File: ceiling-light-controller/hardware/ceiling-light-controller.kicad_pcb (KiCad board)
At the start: 2 copper layers, 15 parts, among them J1 Screw_Terminal_01x03, J2 Screw_Terminal_01x02, Q1 BT136-500, U1 LTV-817, U2 HLK-PM03, U3 MOC3021M, U4 WeMos_mini

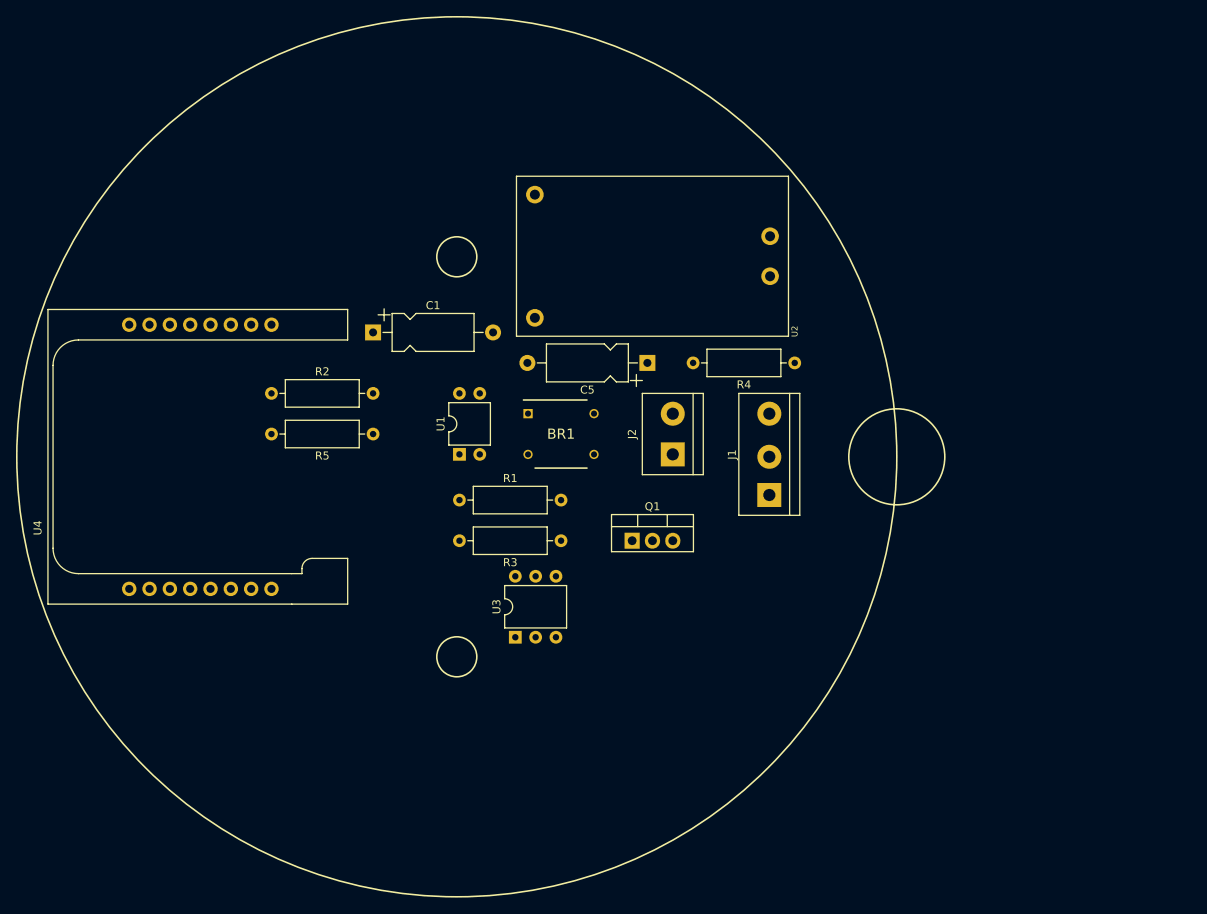
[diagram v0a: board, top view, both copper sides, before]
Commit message: LED, LDR; PCB layout; copper traces
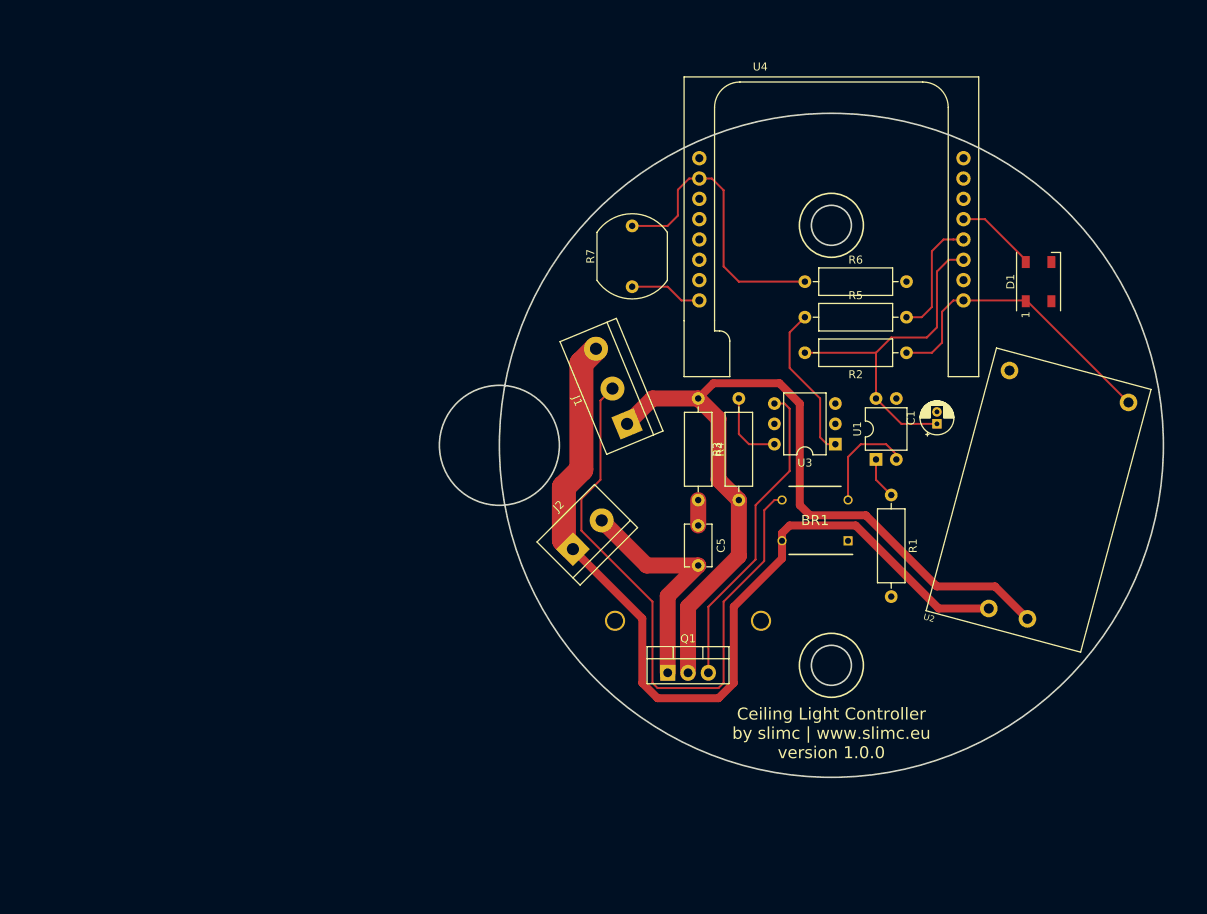
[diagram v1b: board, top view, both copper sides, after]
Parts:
- added D1: WS2812B, LED_SMD:LED_WS2812B_PLCC4_5.0x5.0mm_P3.2mm, F.Cu at (172.7, 78.1)
- added R6: 10000, Resistor_THT:R_Axial_DIN0309_L9.0mm_D3.2mm_P12.70mm_Horizontal, F.Cu at (143.5, 78.1)
- added R7: LDR03, OptoDevice:R_LDR_10x8.5mm_P7.6mm_Vertical, F.Cu at (121.9, 78.7)
- C1: footprint Capacitor_THT:CP_Axial_L10.0mm_D4.5mm_P15.00mm_Horizontal -> Capacitor_THT:CP_Radial_D4.0mm_P1.50mm
- C5: footprint Capacitor_THT:CP_Axial_L10.0mm_D4.5mm_P15.00mm_Horizontal -> Capacitor_THT:C_Disc_D5.1mm_W3.2mm_P5.00mm
- Q1: footprint Package_TO_SOT_THT:TO-220-3_Vertical -> slimc:TO-220-3_Vertical_Triode_Heatsink
- moved U4 83.8 mm to (146.8, 71.6), turned to 90 degrees
- moved R2 79.5 mm to (156.2, 87.0), turned to 180 degrees
- moved C1 71.4 mm to (160.0, 95.9), turned to 90 degrees
- moved U2 57.1 mm to (172.7, 105.4), turned to 75 degrees
- moved R5 55.9 mm to (143.5, 82.5), turned to 0 degrees
- moved R1 54.0 mm to (154.3, 104.8), turned to 270 degrees
- moved U1 52.1 mm to (152.4, 100.3)
- moved U3 46.7 mm to (147.3, 98.4), turned to 180 degrees
- moved BR1 33.5 mm to (144.8, 108.0), turned to 180 degrees
- moved R3 22.8 mm to (135.3, 105.4), turned to 90 degrees
- moved C5 21.3 mm to (130.2, 108.6), turned to 270 degrees
- moved J1 19.9 mm to (121.3, 95.9), turned to 112.5 degrees
- moved J2 17.2 mm to (114.5, 111.5), turned to 45 degrees
- moved Q1 17.1 mm to (126.4, 127.0)
- moved R4 12.9 mm to (130.2, 92.7), turned to 270 degrees
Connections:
- BR1 pad 3: NEUT -> Net-(BR1-Pad3)
- BR1 pad 4: VAC -> Net-(BR1-Pad4)
- C5 pad 2: VAC -> Net-(C5-Pad2)
- J1 pad 1: VAC -> Net-(J1-Pad1)
- J1 pad 2: NEUT -> Net-(BR1-Pad3)
- J1 pad 3: VAC -> Net-(BR1-Pad4)
- J2 pad 1: NEUT -> Net-(BR1-Pad4)
- J2 pad 2: VAC -> Net-(C5-Pad2)
- Q1 pad 1: VAC -> Net-(C5-Pad2)
- Q1 pad 2: VAC -> Net-(J1-Pad1)
- R3 pad 1: VAC -> Net-(J1-Pad1)
- R4 pad 1: VAC -> Net-(J1-Pad1)
- U2 pad 1: NEUT -> Net-(BR1-Pad4)
- U2 pad 2: VAC -> Net-(J1-Pad1)
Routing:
- net Net-(BR1-Pad4): track 0.00 -> 114.8 mm
- net Net-(J1-Pad1): track 0.00 -> 110.8 mm
- net Net-(BR1-Pad3): track 0.00 -> 78.0 mm
- net Net-(C1-Pad1): track 0.00 -> 43.4 mm
- net Net-(Q1-Pad3): track 0.00 -> 39.4 mm
- net Net-(D1-Pad1): track 0.00 -> 38.0 mm
- net Net-(R6-Pad1): track 0.00 -> 36.9 mm
- net Net-(C5-Pad2): track 0.00 -> 29.4 mm
- net Net-(R5-Pad1): track 0.00 -> 19.6 mm
- net Net-(R5-Pad2): track 0.00 -> 15.2 mm
- net Net-(BR1-Pad2): track 0.00 -> 13.2 mm
- net Net-(D1-Pad4): track 0.00 -> 10.2 mm
- net Net-(R3-Pad2): track 0.00 -> 9.42 mm
- net Net-(R7-Pad1): track 0.00 -> 9.11 mm
- net Net-(R1-Pad1): track 0.00 -> 5.23 mm
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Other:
- board outline added: 90.5 x 83 mm
- board text added: "Ceiling Light Controller by slimc | www.slimc.eu version 1.0.0"

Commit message: gerber files and order sample
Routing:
- net Net-(BR1-Pad1): track 0.00 -> 9.70 mm
- added copper zone on B.Cu, net GND
- added copper zone on F.Cu, net GND
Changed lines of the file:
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@@
     (thickness 1.6)
     (drawings 7)
-    (tracks 121)
+    (tracks 125)
     (zones 0)
     (modules 18)
@@
     (visible_elements FFFFFF7F)
     (pcbplotparams
-      (layerselection 0x010fc_ffffffff)
+      (layerselection 0x010a0_ffffffff)
       (usegerberextensions false)
       (usegerberattributes false)
@@
       (outputformat 1)
       (mirror false)
-      (drillshape 1)
+      (drillshape 0)
       (scaleselection 1)
-      (outputdirectory ""))
+      (outputdirectory "gerbers/"))
   )
   (net 0 "")
@@
     )
   )
+  (gr_circle (center 146.825 98.565) (end 188.325 98.565) (layer Edge.Cuts) (width 0.2))
+  (gr_circle (center 105.325 98.565) (end 112.825 98.565) (layer Edge.Cuts) (width 0.2))
   (gr_circle (center 146.825 126.065) (end 150.825 126.065) (layer F.SilkS) (width 0.2))
   (gr_circle (center 146.825 71.065) (end 150.825 71.065) (layer F.SilkS) (width 0.2))
-  (gr_circle (center 105.325 98.565) (end 112.825 98.565) (layer Edge.Cuts) (width 0.2))
   (gr_circle (center 146.825 126.065) (end 149.325 126.065) (layer Edge.Cuts) (width 0.2))
   (gr_circle (center 146.825 71.065) (end 149.325 71.065) (layer Edge.Cuts) (width 0.2))
-  (gr_circle (center 146.825 98.565) (end 188.325 98.565) (layer Edge.Cuts) (width 0.2))
   (gr_text "Ceiling Light Controller\nby slimc | www.slimc.eu\nversion 1.0.0" (at 146.825 134.565) (layer F.SilkS)
     (effects (font (size 1.5 1.5) (thickness 0.3)))
@@
   (segment (start 162.062208 72.835) (end 163.335 72.835) (width 0.25) (layer F.Cu) (net 8))
   (segment (start 158.115 82.55) (end 159.385 81.28) (width 0.25) (layer F.Cu) (net 8))
+  (segment (start 154.305 115.07) (end 154.305 116.34363) (width 0.25) (layer F.Cu) (net 20))
+  (segment (start 154.305 116.34363) (end 154.305 117.475) (width 0.25) (layer F.Cu) (net 20))
+  (segment (start 149.735 110.5) (end 154.305 115.07) (width 0.25) (layer F.Cu) (net 20))
+  (segment (start 148.905 110.5) (end 149.735 110.5) (width 0.25) (layer F.Cu) (net 20))
   (segment (start 154.94 99.695) (end 154.94 100.33) (width 0.25) (layer F.Cu) (net 21))
   (segment (start 153.67 98.425) (end 154.94 99.695) (width 0.25) (layer F.Cu) (net 21))
@@
   (segment (start 139.71 105.4) (end 138.43 106.68) (width 0.25) (layer F.Cu) (net 24))
   (segment (start 138.43 106.68) (end 138.43 113.03) (width 0.25) (layer F.Cu) (net 24))
-  (segment (start 115.57 88.32532) (end 117.396936 86.498384) (width 3) (layer F.Cu) (net 25))
-  (segment (start 113.386528 110.410732) (end 113.386528 103.783472) (width 3) (layer F.Cu) (net 25))
-  (segment (start 114.517898 111.542102) (end 113.386528 110.410732) (width 3) (layer F.Cu) (net 25))
-  (segment (start 115.57 101.6) (end 115.57 88.32532) (width 3) (layer F.Cu) (net 25))
-  (segment (start 113.386528 103.783472) (end 115.57 101.6) (width 3) (layer F.Cu) (net 25))
   (segment (start 114.517898 111.542102) (end 115.649268 112.673472) (width 0.25) (layer F.Cu) (net 25))
   (segment (start 125.09359 130.175) (end 132.71641 130.175) (width 1) (layer F.Cu) (net 25))
@@
   (segment (start 123.19 120.214204) (end 114.517898 111.542102) (width 1) (layer F.Cu) (net 25))
   (segment (start 123.19 128.27) (end 123.19 120.214204) (width 1) (layer F.Cu) (net 25))
+  (segment (start 115.57 101.6) (end 115.57 88.32532) (width 3) (layer F.Cu) (net 25))
+  (segment (start 114.517898 111.542102) (end 113.386528 110.410732) (width 3) (layer F.Cu) (net 25))
+  (segment (start 113.386528 103.783472) (end 115.57 101.6) (width 3) (layer F.Cu) (net 25))
+  (segment (start 113.386528 110.410732) (end 113.386528 103.783472) (width 3) (layer F.Cu) (net 25))
+  (segment (start 115.57 88.32532) (end 117.396936 86.498384) (width 3) (layer F.Cu) (net 25))
   (segment (start 171.02 80.455) (end 171.12 80.555) (width 0.25) (layer F.Cu) (net 26))
   (segment (start 163.335 80.455) (end 171.02 80.455) (width 0.25) (layer F.Cu) (net 26))
@@
   (segment (start 121.92 78.74) (end 126.365 78.74) (width 0.25) (layer F.Cu) (net 30))
   (segment (start 126.365 78.74) (end 128.08 80.455) (width 0.25) (layer F.Cu) (net 30))
+  (zone (net 1) (net_name GND) (layer F.Cu) (hatch edge 0.508)
+    (connect_pads (clearance 0.508))
+    (min_thickness 0.254)
+    (fill (arc_segments 16) (thermal_gap 0.508) (thermal_bridge_width 0.508))
+    (polygon
+      (pts
+        (xy 141.605 88.9) (xy 145.415 92.71) (xy 145.415 102.235) (xy 163.195 102.235) (xy 188.595 109.22)
+        (xy 191.77 94.615) (xy 184.785 65.405) (xy 160.655 50.8) (xy 113.665 53.34) (xy 109.22 75.565)
+        (xy 131.445 88.9)
+      )
+    )
+  )
+  (zone (net 1) (net_name GND) (layer B.Cu) (hatch edge 0.508)
+    (connect_pads (clearance 0.508))
+    (min_thickness 0.254)
+    (fill (arc_segments 16) (thermal_gap 0.508) (thermal_bridge_width 0.508))
+    (polygon
+      (pts
+        (xy 177.165 63.5) (xy 185.42 72.39) (xy 191.77 94.615) (xy 188.595 109.22) (xy 163.195 102.235)
+        (xy 145.415 102.235) (xy 145.415 92.71) (xy 141.605 88.9) (xy 131.445 88.9) (xy 109.22 75.565)
+        (xy 113.665 53.34) (xy 160.655 50.8)
+      )
+    )
+  )
+  (zone (net 0) (net_name "") (layers F&B.Cu) (hatch edge 0.508)
+    (connect_pads (clearance 0.508))
+    (min_thickness 0.254)
+    (keepout (tracks not_allowed) (vias not_allowed) (copperpour allowed))
+    (fill (arc_segments 16) (thermal_gap 0.508) (thermal_bridge_width 0.508))
+    (polygon
+      (pts
+        (xy 112.395 85.09) (xy 120.015 81.915) (xy 123.19 88.9) (xy 141.605 88.9) (xy 145.415 92.71)
+        (xy 145.415 105.41) (xy 151.765 105.41) (xy 160.655 114.3) (xy 168.91 114.3) (xy 173.99 120.015)
+        (xy 173.355 121.92) (xy 171.45 122.555) (xy 169.545 121.92) (xy 168.275 120.65) (xy 155.575 120.65)
+        (xy 145.415 120.65) (xy 141.605 123.19) (xy 141.605 131.445) (xy 118.745 131.445) (xy 109.855 120.015)
+        (xy 109.855 102.235) (xy 112.395 99.695)
+      )
+    )
+  )
 )
